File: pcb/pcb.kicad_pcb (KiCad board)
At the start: 2 copper layers, 63 parts, among them J1 WH, J2 RGB, J3 220, Q1 AO3400A, Q2 AO3400A, Q3 AO3400A, Q4 AO3400A, Q5 2N60, Q6 DTD114E, Q7 AO3400A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

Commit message: pcb ok, code is coming
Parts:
- added T1: ., local:Transformer_NF_ETAL_P1165, B.Cu at (171.6, 149.6)
- C1: footprint Capacitor_THT:C_Axial_L3.8mm_D2.6mm_P7.50mm_Horizontal -> Capacitor_THT:CP_Radial_D13.0mm_P7.50mm; moved to B.Cu
- C11: footprint Capacitor_SMD:C_0805_2012Metric -> Capacitor_SMD:C_0402_1005Metric
- C12, C13, C14, C2, C3, C5, C6, C7, D4, J1, J2, L1, L2, L3, RV1, SW2, TH1: moved to B.Cu
- Q5: value 2N60 -> AOD452; footprint Package_TO_SOT_THT:TO-220-3_Vertical -> Package_TO_SOT_SMD:TO-252-2
- R15: footprint Resistor_SMD:R_0805_2012Metric -> Resistor_SMD:R_0402_1005Metric
- SW1: footprint Button_Switch_THT:SW_PUSH_6mm -> local:SW_PUSH_6mm_2cont; moved to B.Cu
- moved J2 160.0 mm to (229.5, 144.9), turned to 180 degrees
- moved R9 157.3 mm to (219.4, 149.7), turned to -90 degrees
- moved R5 155.4 mm to (218.8, 144.7)
- moved R12 153.6 mm to (226.2, 147.2)
- moved R14 150.0 mm to (226.2, 152.8)
- moved R6 147.8 mm to (218.8, 148.2)
- moved R8 147.5 mm to (219.4, 146.2), turned to -90 degrees
- moved R13 143.7 mm to (226.2, 150.0)
- moved R11 139.5 mm to (215.3, 133.7)
- moved C14 138.6 mm to (226.7, 147.4), turned to 180 degrees
- moved C12 135.2 mm to (226.7, 150.0)
- moved Q5 130.9 mm to (222.1, 137.7)
- moved Q1 125.9 mm to (214.8, 136.2), turned to 90 degrees
- moved D4 119.7 mm to (211.8, 143.3), turned to 180 degrees
- moved R10 119.2 mm to (219.4, 153.3), turned to -90 degrees
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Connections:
- C7 pad 2: Net-(C7-Pad2) -> GND
- D6 pad 2: Net-(C7-Pad2) -> Net-(D6-Pad2)
- D7 pad 2: Net-(C7-Pad2) -> Net-(D6-Pad2)
- L1 pad 2: Net-(D1-Pad3) -> Net-(D1-Pad4)
- L1 pad 4: Net-(D1-Pad4) -> Net-(D1-Pad3)
- Q6 pad 2: Net-(C7-Pad2) -> Net-(D6-Pad2)
- R1 pad 1: Net-(J3-Pad2) -> Net-(J3-Pad1)
- R1 pad 2: Net-(L1-Pad1) -> Net-(L1-Pad3)
- R18 pad 2: Net-(C7-Pad2) -> Net-(D6-Pad2)
- R20 pad 1: Net-(C7-Pad2) -> Net-(D6-Pad2)
- TH1 pad 1: Net-(J3-Pad1) -> Net-(J3-Pad2)
- TH1 pad 2: Net-(L1-Pad3) -> Net-(L1-Pad1)
- U1 pad 1: Net-(SW1-Pad1) -> Net-(R3-Pad2)
- U1 pad 3: Net-(R7-Pad1) -> Net-(SW1-Pad1)
- U1 pad 5: Net-(R3-Pad2) -> Net-(R7-Pad1)
- U1 pad 6: Net-(R5-Pad1) -> Net-(R6-Pad1)
- U1 pad 7: Net-(R6-Pad1) -> Net-(R5-Pad1)
- U4 pad 3: Net-(C7-Pad2) -> Net-(D6-Pad2)
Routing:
- net GND: track 0.00 -> 251.0 mm, vias 0 -> 3
- net +12V: track 0.00 -> 92.9 mm, vias 0 -> 1
- net Net-(C1-Pad2): track 0.00 -> 80.3 mm
- net Net-(C1-Pad1): track 0.00 -> 53.5 mm
- net +5V: track 0.00 -> 43.5 mm, vias 0 -> 2
- net Net-(D3-Pad1): track 0.45 -> 31.9 mm
- net Net-(D6-Pad2): track 0.00 -> 26.4 mm
- net Net-(SW1-Pad3): track 0.00 -> 23.3 mm
- net Net-(SW1-Pad1): track 0.00 -> 21.1 mm
- net Net-(C5-Pad1): track 0.00 -> 20.2 mm
- net Net-(D4-Pad1): track 0.00 -> 18.7 mm
- net Net-(U2-Pad4): track 0.00 -> 18.5 mm
- net Net-(C3-Pad2): track 0.00 -> 13.2 mm
- net Net-(D5-Pad2): track 0.00 -> 12.6 mm
- net Net-(D1-Pad4): track 0.00 -> 10.6 mm
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
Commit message: operate led
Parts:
- added D8: LED, LED_SMD:LED_0603_1608Metric, B.Cu at (109.0, 49.3)
- added R21: 1k, Resistor_SMD:R_0402_1005Metric, B.Cu at (108.1, 47.4)
- moved C1 134.3 mm to (64.8, 37.8)
- moved C10 134.3 mm to (129.6, 37.9)
- moved C3 134.3 mm to (83.3, 28.6)
- moved C5 134.3 mm to (125.3, 29.4)
- moved C7 134.3 mm to (114.7, 30.1)
- moved J2 134.3 mm to (144.9, 40.7)
- moved L2 134.3 mm to (137.2, 38.3)
- moved L3 134.3 mm to (100.7, 41.5)
- moved Q1 134.3 mm to (130.1, 32.0)
- moved Q2 134.3 mm to (137.2, 41.5)
- moved Q4 134.3 mm to (137.2, 48.6)
- moved R19 134.3 mm to (102.3, 35.8)
- moved R6 134.3 mm to (134.2, 44.0)
- moved R8 134.3 mm to (134.7, 42.0)
- moved RV1 134.3 mm to (43.2, 36.2)
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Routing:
- net GND: track 251.0 -> 369.6 mm, vias 3 -> 2
- net +12V: track 92.9 -> 113.9 mm
- net Net-(D5-Pad2): track 12.6 -> 25.5 mm
- net Net-(D4-Pad1): track 18.7 -> 8.96 mm
- net Net-(C3-Pad2): track 13.2 -> 22.4 mm
- net +5V: track 43.5 -> 36.9 mm
- net Net-(C1-Pad1): track 53.5 -> 58.8 mm, vias 0 -> 1
- net Net-(D8-Pad2): track 0.00 -> 1.43 mm
- net Net-(D1-Pad4): track 10.6 -> 9.29 mm
- net Net-(D1-Pad3): track 6.85 -> 5.65 mm
- net Net-(C1-Pad2): track 80.3 -> 79.4 mm
- net Net-(U2-Pad4): track 18.5 -> 17.7 mm

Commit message: -2cm
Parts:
- moved SW2 26.2 mm to (100.8, 48.7)
- moved C6 18.5 mm to (119.0, 39.4), turned to 180 degrees
- moved D8 18.4 mm to (127.4, 49.0)
- moved R21 18.4 mm to (126.6, 47.1)
- moved C7 13.2 mm to (110.8, 42.8)
- moved R4 11.5 mm to (118.2, 34.6)
- moved Q1 11.5 mm to (118.7, 32.0)
- moved R3 11.0 mm to (117.7, 36.1), turned to -90 degrees
- moved R5 10.9 mm to (123.3, 39.8)
- moved U1 10.9 mm to (118.6, 40.0)
- moved R7 10.5 mm to (123.8, 46.4), turned to -90 degrees
- moved C12 10.4 mm to (131.7, 45.8)
- moved C13 10.4 mm to (131.7, 48.3)
- moved C14 10.4 mm to (131.7, 43.2)
- moved J1 10.4 mm to (134.5, 28.2)
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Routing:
- net Net-(SW1-Pad3): track 23.6 -> 40.9 mm
- net GND: track 369.6 -> 386.1 mm, vias 2 -> 1
- net Net-(SW1-Pad1): track 21.1 -> 36.0 mm
- net Net-(C5-Pad1): track 20.0 -> 30.8 mm
- net +5V: track 36.9 -> 28.1 mm
- net +12V: track 113.9 -> 122.1 mm
- net Net-(U2-Pad4): track 17.7 -> 10.9 mm
- net Net-(C1-Pad2): track 79.4 -> 73.9 mm
- net Net-(D3-Pad1): track 31.9 -> 37.0 mm
- net Net-(D6-Pad2): track 26.4 -> 31.0 mm
- net Net-(D5-Pad2): track 25.5 -> 21.7 mm
- net Net-(Q3-Pad1): track 2.64 -> 4.75 mm
- net Net-(R3-Pad2): track 4.40 -> 2.98 mm
- net Net-(Q4-Pad1): track 2.64 -> 4.05 mm
- net Net-(D2-Pad2): track 5.10 -> 6.40 mm
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
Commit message: err in sch, some code added
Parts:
- added R22: 10k, Resistor_SMD:R_0402_1005Metric, B.Cu at (110.1, 37.2)
- added R23: 10k, Resistor_SMD:R_0402_1005Metric, F.Cu at (100.8, 46.8)
- added R24: 10k, Resistor_SMD:R_0402_1005Metric, F.Cu at (106.3, 48.7)
- added R25: 10k, Resistor_SMD:R_0402_1005Metric, F.Cu at (106.3, 50.1)
- D8: value LED -> pwr_ok
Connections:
- SW1 pad 1: Net-(SW1-Pad1) -> Net-(U1-Pad2)
- SW1 pad 3: Net-(SW1-Pad3) -> Net-(U1-Pad2)
- SW2 pad A: Net-(SW1-Pad3) -> Net-(U1-Pad3)
- SW2 pad B: Net-(SW1-Pad1) -> Net-(SW2-PadB)
- SW2 pad C: GND -> Net-(SW2-PadC)
- U1 pad 2: Net-(SW1-Pad3) -> Net-(U1-Pad2)
- U1 pad 3: Net-(SW1-Pad1) -> Net-(U1-Pad3)
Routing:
- net GND: track 386.1 -> 321.7 mm
- net Net-(SW1-Pad3): track 40.9 -> 0.00 mm
- net Net-(SW1-Pad1): track 36.0 -> 0.00 mm
- net Net-(U1-Pad3): track 0.00 -> 35.1 mm, vias 0 -> 1
- net Net-(U1-Pad2): track 0.00 -> 20.6 mm
- net Net-(SW2-PadB): track 0.00 -> 10.5 mm
- net Net-(SW2-PadC): track 0.00 -> 6.72 mm
- net Net-(C1-Pad2): track 73.9 -> 79.1 mm
- net +12V: track 122.1 -> 127.1 mm
- net +5V: track 28.1 -> 29.4 mm
- net Net-(D6-Pad2): track 31.0 -> 31.8 mm

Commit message: light sensor added completely
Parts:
- added R26: R_Photo, LED_THT:LED_D3.0mm, B.Cu at (104.9, 45.6)
- D4: moved to F.Cu
- moved D4 9.91 mm to (134.5, 35.3), turned to 90 degrees
- moved U1 0.43 mm to (119.0, 40.0)
- moved R5 0.10 mm to (123.3, 39.9), turned to -90 degrees
- moved R23 0.08 mm to (100.8, 46.9)
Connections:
- R22 pad 2: Net-(U1-Pad3) -> Net-(R22-Pad2)
- R23 pad 1: Net-(U1-Pad3) -> Net-(R22-Pad2)
- SW1 pad 1: Net-(U1-Pad2) -> Net-(R22-Pad2)
- SW1 pad 3: Net-(U1-Pad2) -> Net-(R22-Pad2)
- SW2 pad A: Net-(U1-Pad3) -> Net-(R22-Pad2)
- U1 pad 3: Net-(U1-Pad3) -> Net-(R22-Pad2)
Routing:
- net Net-(R22-Pad2): track 0.00 -> 64.2 mm
- net Net-(U1-Pad3): track 35.1 -> 0.00 mm, vias 1 -> 0
- net Net-(D3-Pad1): track 37.0 -> 56.5 mm, vias 0 -> 2
- net Net-(D4-Pad1): track 8.86 -> 14.7 mm
- net Net-(U1-Pad2): track 20.6 -> 16.3 mm, vias 0 -> 1
- net Net-(D6-Pad2): track 31.8 -> 29.8 mm
- net GND: track 321.7 -> 323.1 mm
- net +5V: track 29.4 -> 30.8 mm
- net Net-(R8-Pad1): track 3.23 -> 3.94 mm

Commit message: -0.5 cm
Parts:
- C1: footprint Capacitor_THT:CP_Radial_D13.0mm_P7.50mm -> Capacitor_THT:CP_Radial_D10.0mm_P7.50mm; moved to F.Cu
- L1: footprint Inductor_THT:Choke_Schaffner_RN212-04-12.5x18.0mm -> local:Input_coil; moved to F.Cu
- moved R1 21.0 mm to (51.3, 48.5)
- moved L1 17.4 mm to (63.9, 44.7), turned to 90 degrees
- moved TH1 17.0 mm to (53.0, 28.4)
- moved J3 16.0 mm to (50.2, 44.2), turned to 90 degrees
- moved RV1 10.8 mm to (53.0, 41.0), turned to -90 degrees
- moved C1 7.13 mm to (67.6, 32.9), turned to 180 degrees
- moved D1 6.00 mm to (63.9, 37.1), turned to -90 degrees
- moved C4 0.71 mm to (71.9, 45.4)
- moved U2 0.69 mm to (74.4, 38.8)
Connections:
- L1 pad 1: Net-(L1-Pad1) -> Net-(TH1-Pad2)
- L1 pad 3: Net-(L1-Pad3) -> Net-(R1-Pad2)
- R1 pad 2: Net-(L1-Pad3) -> Net-(R1-Pad2)
- RV1 pad 1: Net-(J3-Pad2) -> Net-(TH1-Pad2)
- RV1 pad 2: Net-(J3-Pad1) -> Net-(R1-Pad2)
- TH1 pad 2: Net-(L1-Pad1) -> Net-(TH1-Pad2)
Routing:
- net Net-(TH1-Pad2): track 0.00 -> 26.2 mm
- net Net-(C1-Pad2): track 79.1 -> 64.2 mm
- net Net-(C1-Pad1): track 58.6 -> 48.4 mm
- net Net-(D1-Pad4): track 9.35 -> 1.59 mm
- net Net-(R1-Pad2): track 0.00 -> 7.24 mm
- net Net-(L1-Pad1): track 5.32 -> 0.00 mm
- net Net-(J3-Pad2): track 9.81 -> 14.7 mm
- net Net-(D1-Pad3): track 5.70 -> 1.59 mm
- net Net-(J3-Pad1): track 8.24 -> 4.45 mm
- net Net-(L1-Pad3): track 2.86 -> 0.00 mm

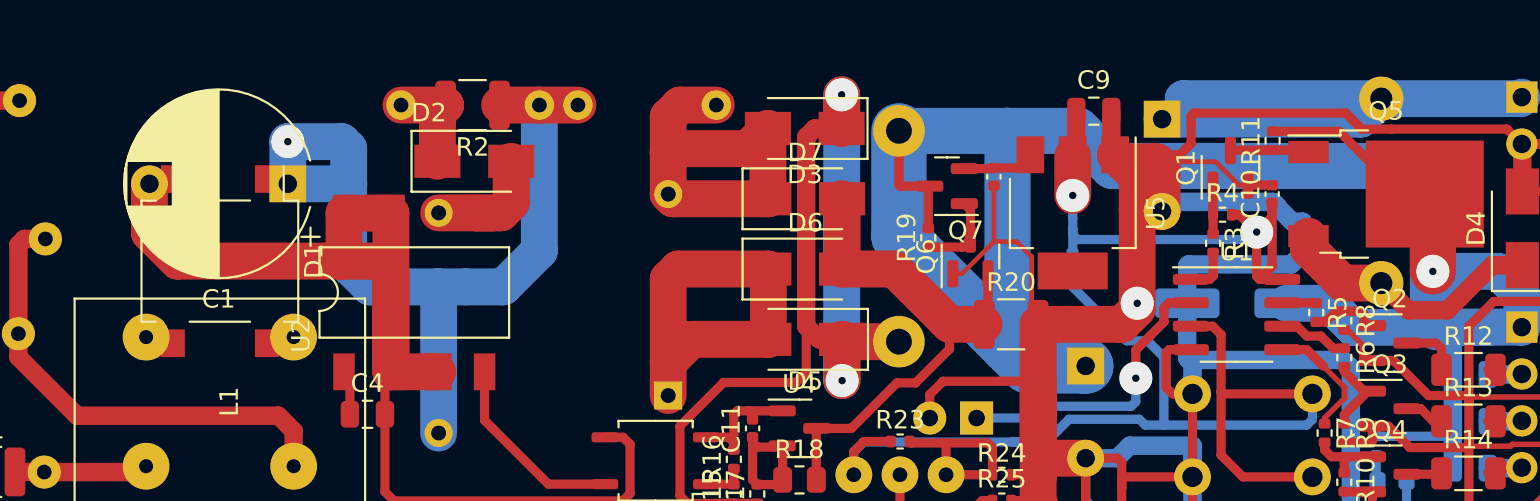
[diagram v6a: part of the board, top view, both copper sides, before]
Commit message: mosfet bootstrap circuit
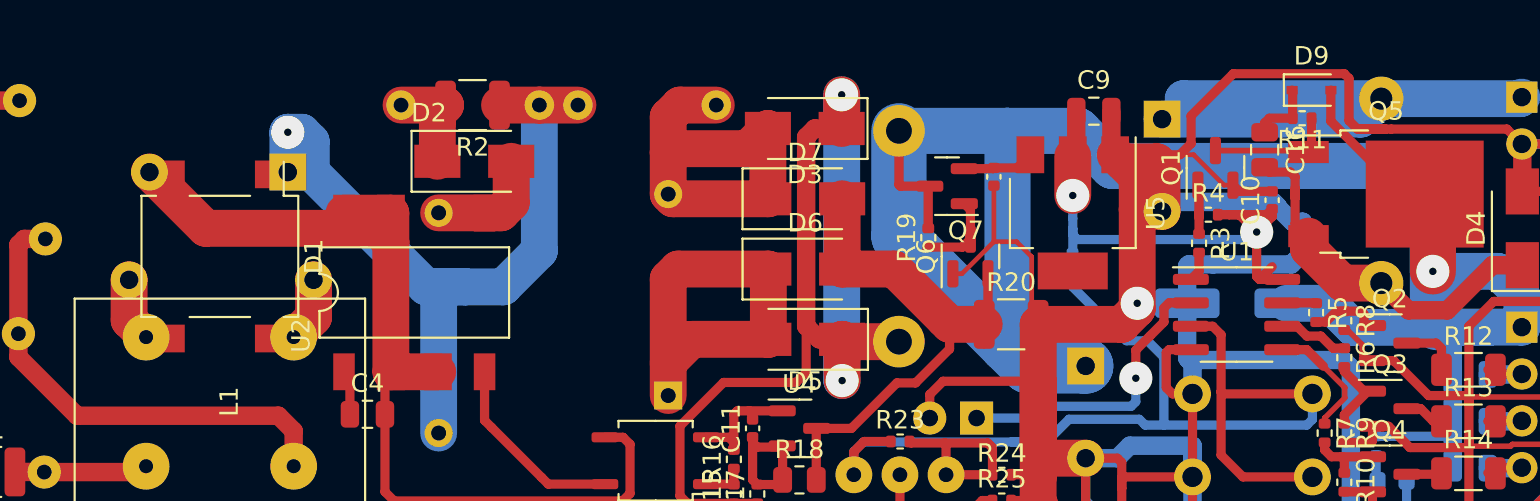
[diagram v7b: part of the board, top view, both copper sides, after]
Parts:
- added C15: 0.1, Capacitor_THT:C_Disc_D11.0mm_W5.0mm_P10.00mm, B.Cu at (69.0, 38.1)
- added C16: 10uF, Capacitor_SMD:C_0805_2012Metric, F.Cu at (120.5, 31.0)
- added D9: 1N5822, Diode_SMD:D_SOD-323, F.Cu at (123.1, 27.8)
- C1: moved to B.Cu
- moved R11 2.01 mm to (122.6, 29.3), turned to 180 degrees
- moved Q1 0.81 mm to (117.9, 32.0)
- moved R3 0.76 mm to (117.0, 36.1)
- moved R4 0.76 mm to (117.5, 34.6)
- moved C1 0.63 mm to (67.6, 32.3)
- moved C10 0.33 mm to (120.9, 33.8)
- moved D1 0.25 mm to (63.9, 36.8)
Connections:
- R11 pad 2: +12V -> Net-(R11-Pad2)
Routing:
- net Net-(C1-Pad2): track 64.2 -> 54.2 mm
- net Net-(D4-Pad1): track 14.7 -> 20.6 mm
- net GND: track 323.1 -> 328.4 mm
- net Net-(R11-Pad2): track 0.00 -> 3.67 mm
- net Net-(C15-Pad1): track 1.59 -> 5.03 mm
- net Net-(C15-Pad2): track 1.59 -> 4.97 mm
- net Net-(C1-Pad1): track 48.4 -> 45.1 mm
- net Net-(Q1-Pad3): track 4.39 -> 7.08 mm
- net Net-(R3-Pad2): track 2.98 -> 1.63 mm
- net +5V: track 30.8 -> 30.2 mm
